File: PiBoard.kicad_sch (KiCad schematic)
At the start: 0 parts

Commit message: small changes for ravi
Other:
- note added: "Connectors ------- FAN"
- note removed: "Connectors ------- FAN Battery"

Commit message: silly mistake
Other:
- sheet CarCAN ports: added none; removed CAN_RESET
- note added: "Connectors ------- CAN Connector"
- note added: "Connectors ------- Fusebox Connector"

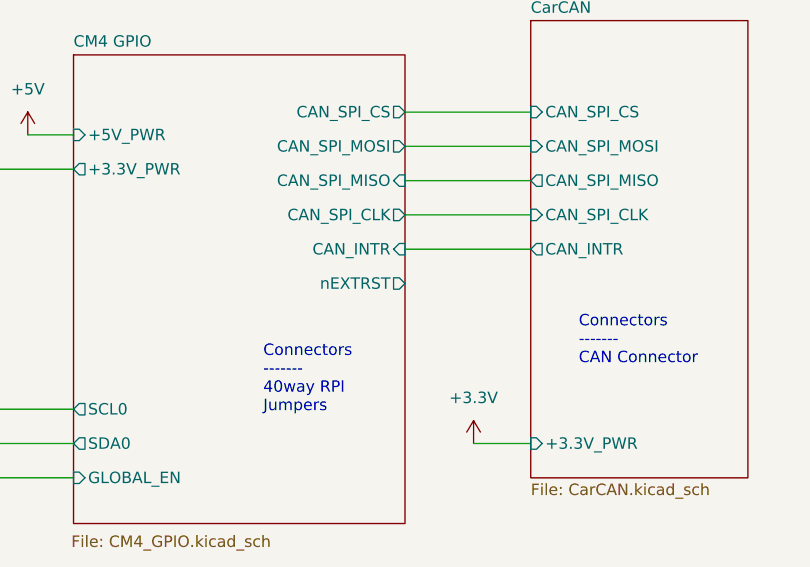
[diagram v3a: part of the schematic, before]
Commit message: added parts to almost everything (except can xtal and fuses)
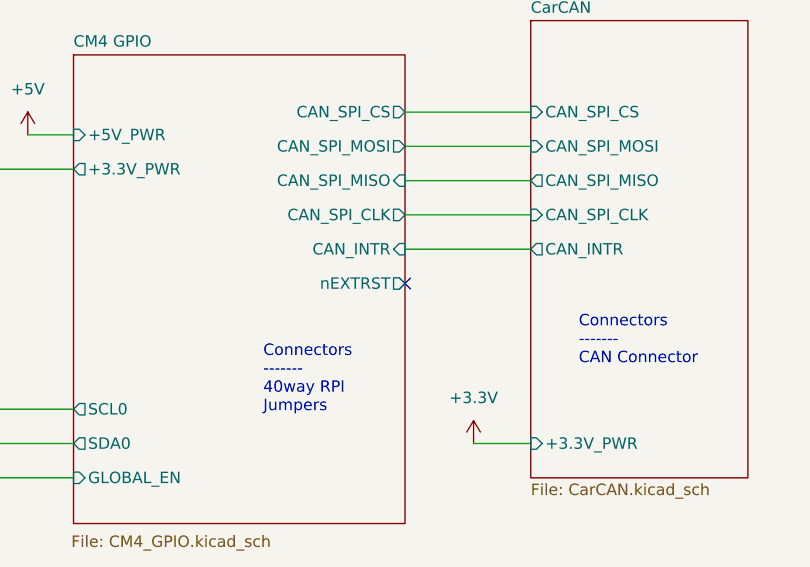
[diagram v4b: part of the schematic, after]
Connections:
- no-connect marks 0 -> 1
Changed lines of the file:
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@@
 	(generator_version "8.0")
 	(paper "A4")
+	(no_connect
+		(at 153.67 113.03)
+	)
 	(wire
 		(pts

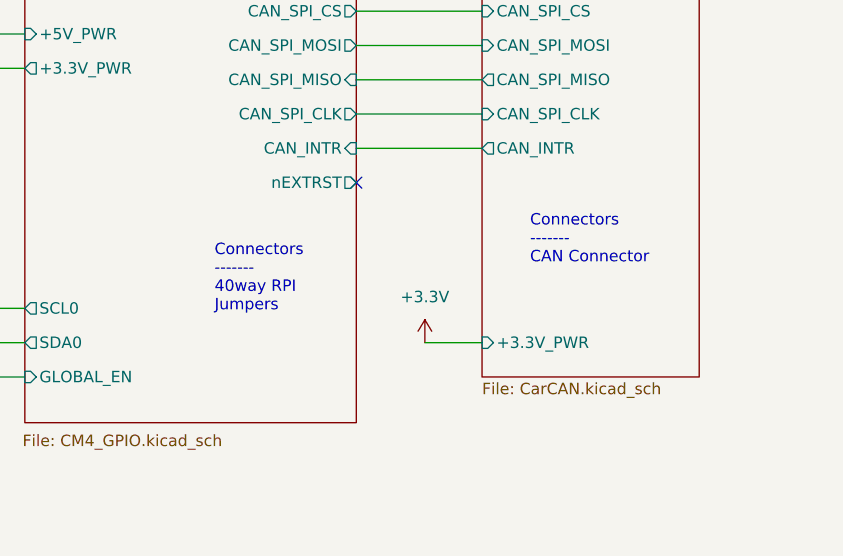
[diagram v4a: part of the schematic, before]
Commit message: fixed cap sizes, added remaining parts, fixed rtc battery
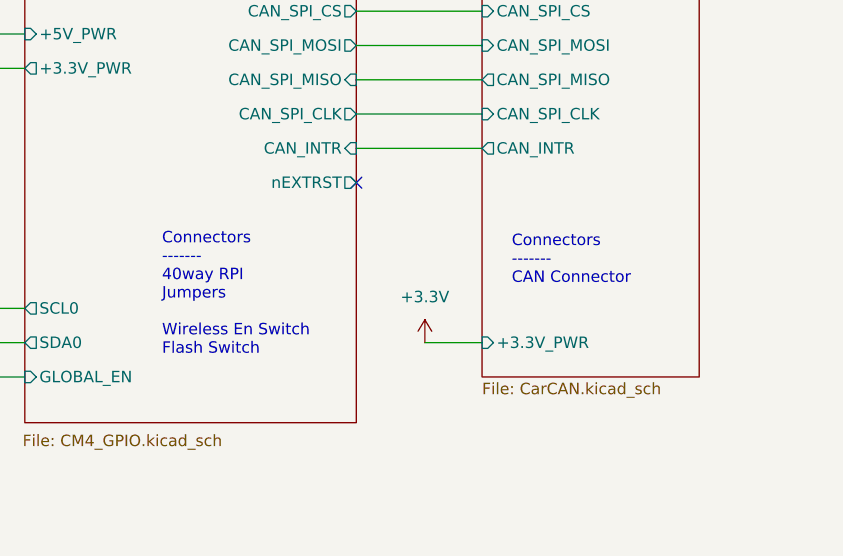
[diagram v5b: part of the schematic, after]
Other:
- note added: "Connectors ------- 40way RPI Jumpers Wireless En Switch Flash Switch"
- note removed: "Connectors ------- 40way RPI Jumpers"
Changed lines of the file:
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@@
 	(text "Connectors\n-------\nCAN Connector"
 		(exclude_from_sim no)
-		(at 172.974 122.174 0)
+		(at 170.942 124.46 0)
 		(effects
 			(font
@@
 		)
 	)
-	(text "Connectors\n-------\n40way RPI\nJumpers"
+	(text "Connectors\n-------\n40way RPI\nJumpers\n\nWireless En Switch\nFlash Switch"
 		(exclude_from_sim no)
-		(at 137.922 127.508 0)
+		(at 132.08 132.334 0)
 		(effects
 			(font

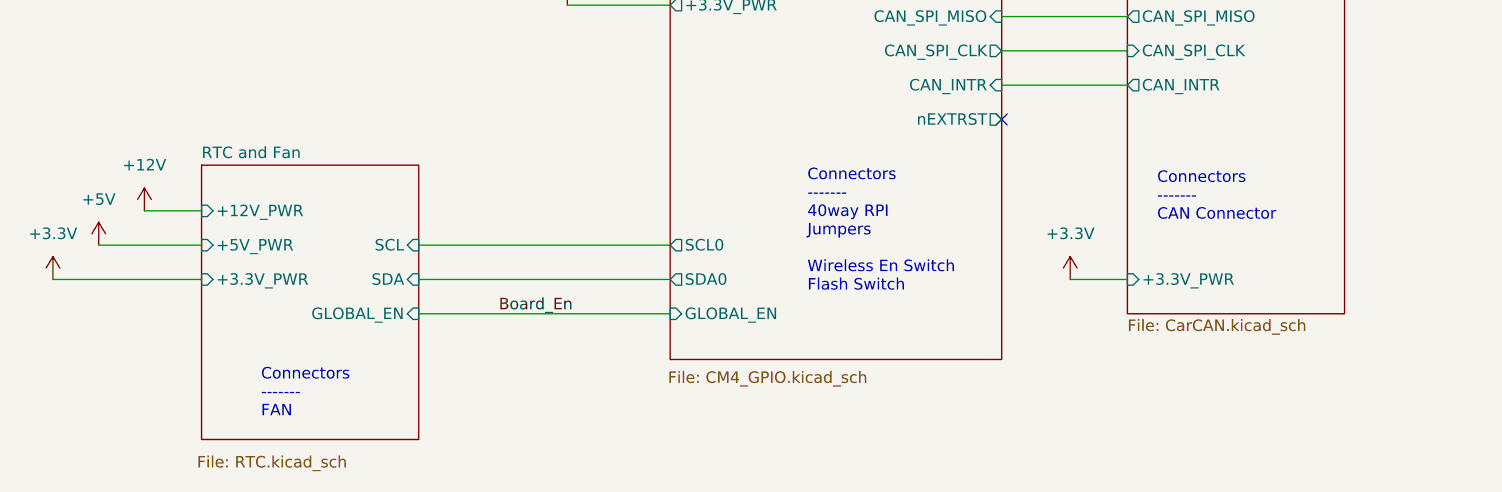
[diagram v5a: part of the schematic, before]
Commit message: fixed relevant erc errors
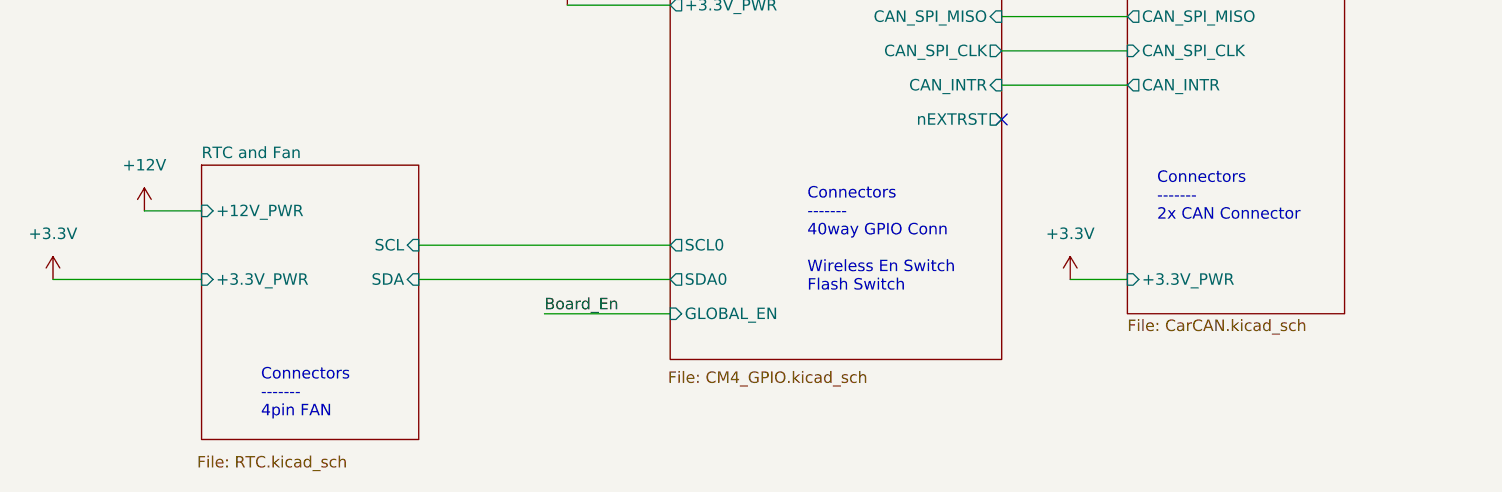
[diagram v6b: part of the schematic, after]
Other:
- sheet RTC and Fan ports: added none; removed +5V_PWR, GLOBAL_EN
- note added: "Connectors ------- 2x CAN Connector"
- note added: "Connectors ------- 40way GPIO Conn Wireless En Switch Flash Switch"
- note added: "Connectors ------- 4pin FAN"
- note removed: "Connectors ------- 40way RPI Jumpers Wireless En Switch Flash Switch"
- note removed: "Connectors ------- CAN Connector"
- note removed: "Connectors ------- FAN"
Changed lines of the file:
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@@
 	(wire
 		(pts
-			(xy 88.9 134.62) (xy 116.84 134.62)
+			(xy 102.87 134.62) (xy 116.84 134.62)
 		)
 		(stroke
@@
 		(pts
 			(xy 88.9 130.81) (xy 116.84 130.81)
-		)
-		(stroke
-			(width 0)
-			(type default)
-		)
-	)
-	(wire
-		(pts
-			(xy 53.34 127) (xy 64.77 127)
 		)
 		(stroke
@@
 		)
 	)
-	(text "Connectors\n-------\nCAN Connector"
+	(text "Connectors\n-------\n2x CAN Connector"
 		(exclude_from_sim no)
 		(at 170.942 124.46 0)
@@
 		)
 	)
-	(text "Connectors\n-------\n40way RPI\nJumpers\n\nWireless En Switch\nFlash Switch"
+	(text "Connectors\n-------\n40way GPIO Conn\n\nWireless En Switch\nFlash Switch"
 		(exclude_from_sim no)
 		(at 132.08 132.334 0)
@@
 		)
 	)
-	(text "Connectors\n-------\nFAN"
+	(text "Connectors\n-------\n4pin FAN"
 		(exclude_from_sim no)
 		(at 71.374 146.304 0)
@@
 	)
 	(label "Board_En"
-		(at 97.79 134.62 0)
+		(at 102.87 134.62 0)
 		(effects
 			(font
@@
 	)
 	(symbol
-		(lib_id "power:+5V")
-		(at 53.34 127 0)
-		(unit 1)
-		(exclude_from_sim no)
-		(in_bom yes)
-		(on_board yes)
-		(dnp no)
-		(fields_autoplaced yes)
-		(property "Reference" "#PWR077"
-			(at 53.34 130.81 0)
-			(effects
-				(font
-					(size 1.27 1.27)
-				)
-				(hide yes)
-			)
-		)
-		(property "Value" "+5V"
-			(at 53.34 121.92 0)
-			(effects
-				(font
-					(size 1.27 1.27)
-				)
-			)
-		)
-		(property "Footprint" ""
-			(at 53.34 127 0)
-			(effects
-				(font
-					(size 1.27 1.27)
-				)
-				(hide yes)
-			)
-		)
-		(property "Datasheet" ""
-			(at 53.34 127 0)
-			(effects
-				(font
-					(size 1.27 1.27)
-				)
-				(hide yes)
-			)
-		)
-		(property "Description" "Power symbol creates a global label with name \"+5V\""
-			(at 53.34 127 0)
-			(effects
-				(font
-					(size 1.27 1.27)
-				)
-				(hide yes)
-			)
-		)
-		(pin "1"
-		)
-		(instances
-			(project "PiBoard"
-				(path "/e4d65698-b8ec-4bf6-9f2b-a5010377155a"
-					(reference "#PWR077")
-					(unit 1)
-				)
-			)
-		)
-	)
-	(symbol
 		(lib_id "power:+3.3V")
 		(at 48.26 130.81 0)
@@
 			)
 		)
-		(pin "GLOBAL_EN" input
-			(at 88.9 134.62 0)
-			(effects
-				(font
-					(size 1.27 1.27)
-				)
-				(justify right)
-			)
-		)
 		(pin "+3.3V_PWR" input
 			(at 64.77 130.81 180)
 			(effects
 				(font
-					(size 1.27 1.27)
-				)
-				(justify left)
-			)
-		)
-		(pin "+5V_PWR" input
-			(at 64.77 127 180)
-			(effects
-				(font

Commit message: moved some stuff around
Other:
- sheet Power Distribution ports: added +24V_PWR; removed +12V_PWR
- sheet RTC and Fan ports: added +24V_PWR; removed +12V_PWR
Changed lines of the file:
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@@
 		(on_board yes)
 		(dnp no)
-		(fields_autoplaced yes)
 		(property "Reference" "#PWR066"
 			(at 77.47 48.26 0)
@@
 			)
 		)
-		(property "Value" "+12V"
-			(at 77.47 39.37 0)
-			(effects
-				(font
-					(size 1.27 1.27)
-				)
+		(property "Value" "+24V"
+			(at 74.676 40.386 0)
+			(effects
+				(font
+					(size 1.27 1.27)
+				)
+				(justify left)
 			)
 		)
@@
 			)
 		)
-		(property "Value" "+12V"
+		(property "Value" "+24V"
 			(at 58.42 118.11 0)
 			(effects
@@
 			)
 		)
-		(pin "+12V_PWR" output
+		(pin "+24V_PWR" output
 			(at 71.12 44.45 0)
 			(effects
@@
 			)
 		)
-		(pin "+12V_PWR" input
+		(pin "+24V_PWR" input
 			(at 64.77 123.19 180)
 			(effects
